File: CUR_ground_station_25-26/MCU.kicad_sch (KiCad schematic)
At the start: 13 parts, among them J4 Conn_01x04_Pin, SW7 PTS815SJM250SMTRLFS, SW8 PTS815SJM250SMTRLFS, U1 ESP32-S3-MINI-1

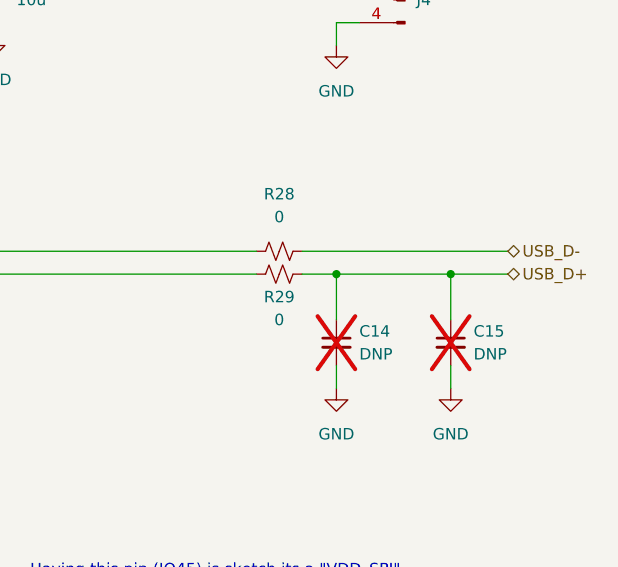
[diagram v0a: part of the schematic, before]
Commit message: Fix USB capacitors
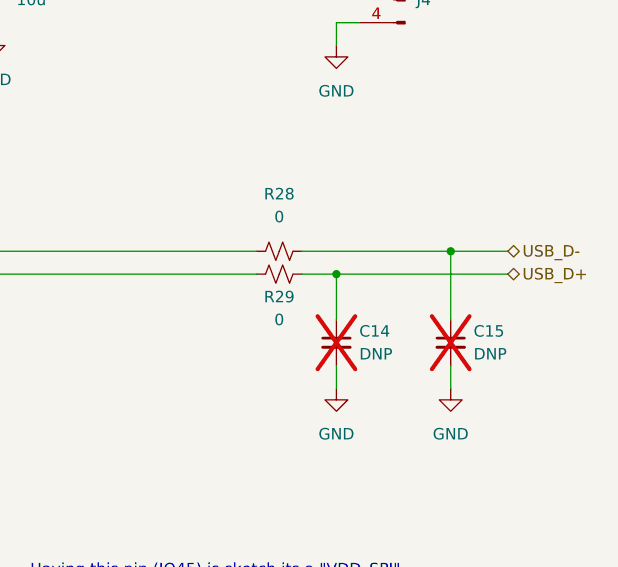
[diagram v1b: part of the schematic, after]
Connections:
- net USB_D+: no longer C15.1
- net USB_D-: now also C15.1
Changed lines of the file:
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@@
+	)
+	(junction
+		(at 234.95 86.36)
+		(diameter 0)
+		(color 0 0 0 0)
 	)
 	(junction
@@
 	)
 	(junction
-		(at 234.95 88.9)
-		(diameter 0)
-		(color 0 0 0 0)
-	)
-	(junction
 		(at 222.25 88.9)
 		(diameter 0)
@@
 	(wire
 		(pts
+			(xy 234.95 86.36) (xy 241.3 86.36)
+		)
+		(stroke
+			(width 0)
+			(type default)
+		)
+	)
+	(wire
+		(pts
 			(xy 130.81 96.52) (xy 137.16 96.52)
 		)
@@
 	(wire
 		(pts
-			(xy 222.25 88.9) (xy 234.95 88.9)
-		)
-		(stroke
-			(width 0)
-			(type default)
-		)
-	)
-	(wire
-		(pts
-			(xy 234.95 88.9) (xy 241.3 88.9)
+			(xy 222.25 88.9) (xy 241.3 88.9)
 		)
 		(stroke
@@
 	(wire
 		(pts
-			(xy 234.95 93.98) (xy 234.95 88.9)
-		)
-		(stroke
-			(width 0)
-			(type default)
-		)
-	)
-	(wire
-		(pts
 			(xy 167.64 104.14) (xy 172.72 104.14)
 		)
@@
 	(wire
 		(pts
+			(xy 234.95 86.36) (xy 234.95 93.98)
+		)
+		(stroke
+			(width 0)
+			(type default)
+		)
+	)
+	(wire
+		(pts
 			(xy 127 78.74) (xy 137.16 78.74)
 		)
@@
 	(wire
 		(pts
-			(xy 218.44 86.36) (xy 241.3 86.36)
-		)
-		(stroke
+			(xy 218.44 86.36) (xy 234.95 86.36)
+		)
+		(stroke

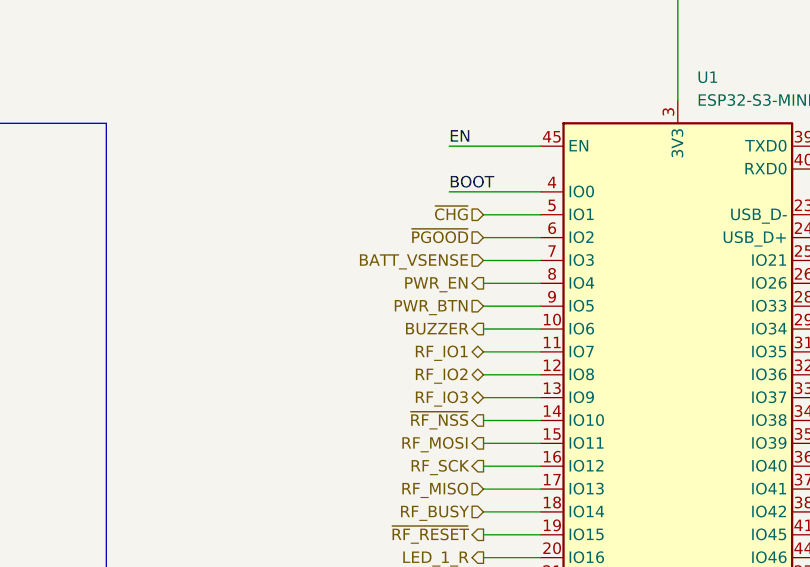
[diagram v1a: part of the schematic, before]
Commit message: switched battery connector, put mounting holes in place
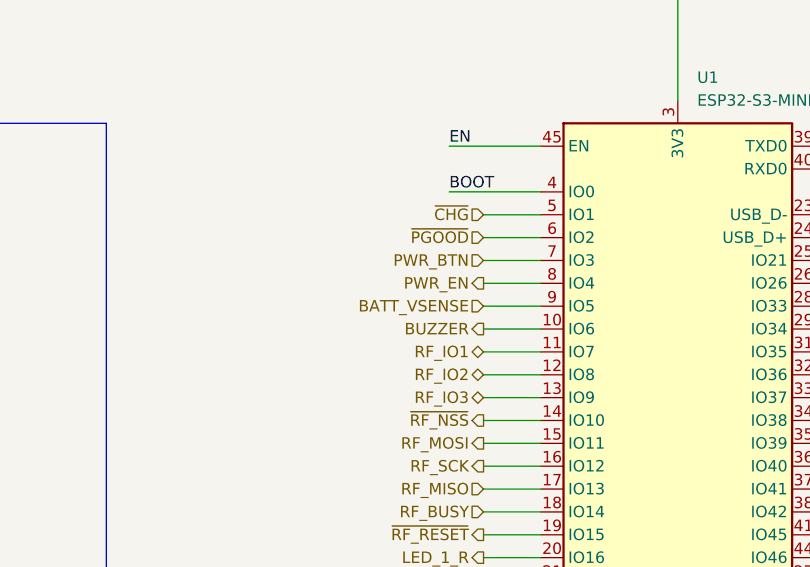
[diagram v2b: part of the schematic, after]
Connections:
- net BATT_VSENSE: now also U1.9 (IO5); no longer U1.7 (IO3)
- net PWR_BTN: now also U1.7 (IO3); no longer U1.9 (IO5)
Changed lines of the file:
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@@
 		)
 	)
-	(hierarchical_label "PWR_BTN"
+	(hierarchical_label "LED_1_B"
+		(shape output)
+		(at 130.81 129.54 180)
+		(effects
+			(font
+				(size 1.27 1.27)
+			)
+			(justify right)
+		)
+	)
+	(hierarchical_label "DISP_~{RES}"
+		(shape output)
+		(at 172.72 116.84 0)
+		(effects
+			(font
+				(size 1.27 1.27)
+			)
+			(justify left)
+		)
+	)
+	(hierarchical_label "DISP_SCL"
+		(shape output)
+		(at 172.72 109.22 0)
+		(effects
+			(font
+				(size 1.27 1.27)
+			)
+			(justify left)
+		)
+	)
+	(hierarchical_label "BTN_3"
+		(shape input)
+		(at 172.72 127 0)
+		(effects
+			(font
+				(size 1.27 1.27)
+			)
+			(justify left)
+		)
+	)
+	(hierarchical_label "RF_MISO"
+		(shape input)
+		(at 130.81 116.84 180)
+		(effects
+			(font
+				(size 1.27 1.27)
+			)
+			(justify right)
+		)
+	)
+	(hierarchical_label "BATT_VSENSE"
 		(shape input)
 		(at 130.81 96.52 180)
-		(effects
-			(font
-				(size 1.27 1.27)
-			)
-			(justify right)
-		)
-	)
-	(hierarchical_label "LED_1_B"
-		(shape output)
-		(at 130.81 129.54 180)
-		(effects
-			(font
-				(size 1.27 1.27)
-			)
-			(justify right)
-		)
-	)
-	(hierarchical_label "DISP_~{RES}"
-		(shape output)
-		(at 172.72 116.84 0)
-		(effects
-			(font
-				(size 1.27 1.27)
-			)
-			(justify left)
-		)
-	)
-	(hierarchical_label "DISP_SCL"
-		(shape output)
-		(at 172.72 109.22 0)
-		(effects
-			(font
-				(size 1.27 1.27)
-			)
-			(justify left)
-		)
-	)
-	(hierarchical_label "BTN_3"
-		(shape input)
-		(at 172.72 127 0)
-		(effects
-			(font
-				(size 1.27 1.27)
-			)
-			(justify left)
-		)
-	)
-	(hierarchical_label "RF_MISO"
-		(shape input)
-		(at 130.81 116.84 180)
 		(effects
 			(font
@@
 		)
 	)
-	(hierarchical_label "BATT_VSENSE"
+	(hierarchical_label "RF_TXEN"
+		(shape input)
+		(at 172.72 93.98 0)
+		(effects
+			(font
+				(size 1.27 1.27)
+			)
+			(justify left)
+		)
+	)
+	(hierarchical_label "DISP_BUSY"
+		(shape input)
+		(at 172.72 114.3 0)
+		(effects
+			(font
+				(size 1.27 1.27)
+			)
+			(justify left)
+		)
+	)
+	(hierarchical_label "LED_2_B"
+		(shape output)
+		(at 172.72 101.6 0)
+		(effects
+			(font
+				(size 1.27 1.27)
+			)
+			(justify left)
+		)
+	)
+	(hierarchical_label "PWR_BTN"
 		(shape input)
 		(at 130.81 91.44 180)
@@
 		)
 	)
-	(hierarchical_label "RF_TXEN"
-		(shape input)
-		(at 172.72 93.98 0)
-		(effects
-			(font
-				(size 1.27 1.27)
-			)
-			(justify left)
-		)
-	)
-	(hierarchical_label "DISP_BUSY"
-		(shape input)
-		(at 172.72 114.3 0)
-		(effects
-			(font
-				(size 1.27 1.27)
-			)
-			(justify left)
-		)
-	)
-	(hierarchical_label "LED_2_B"
-		(shape output)
-		(at 172.72 101.6 0)
-		(effects
-			(font
-				(size 1.27 1.27)
-			)
-			(justify left)
-		)
-	)

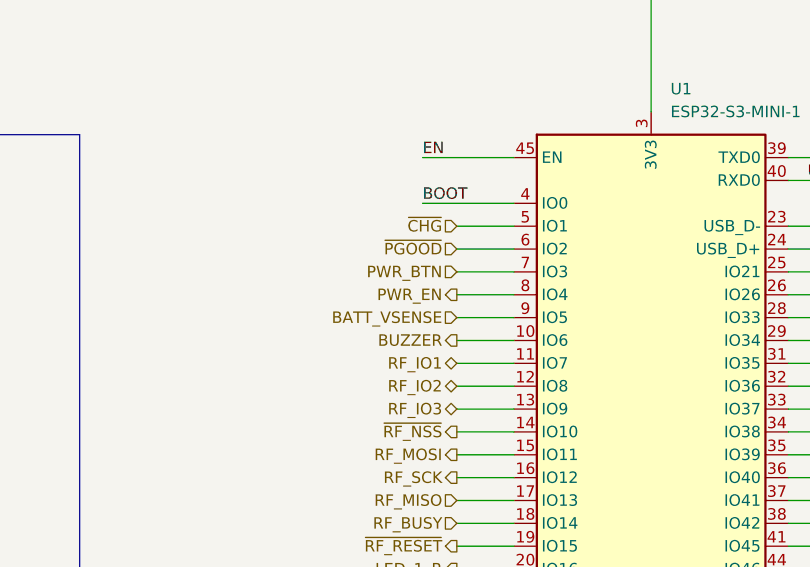
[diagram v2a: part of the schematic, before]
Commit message: routing power section
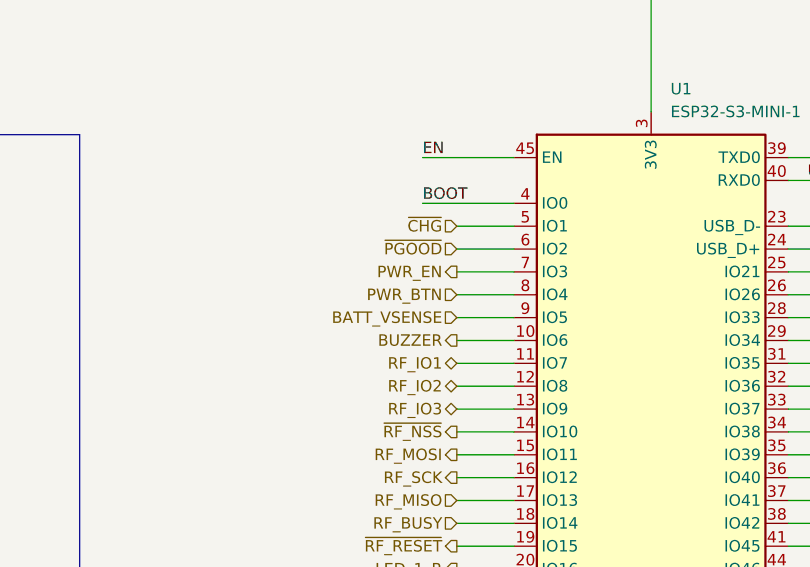
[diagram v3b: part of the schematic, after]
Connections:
- net PWR_BTN: now also U1.8 (IO4); no longer U1.7 (IO3)
- net PWR_EN: now also U1.7 (IO3); no longer U1.8 (IO4)
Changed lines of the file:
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@@
-		)
-	)
-	(hierarchical_label "PWR_BTN"
-		(shape input)
-		(at 130.81 91.44 180)
-		(effects
-			(font
-				(size 1.27 1.27)
-			)
-			(justify right)
 		)
 	)
@@
 		(shape output)
 		(at 130.81 127 180)
+		(effects
+			(font
+				(size 1.27 1.27)
+			)
+			(justify right)
+		)
+	)
+	(hierarchical_label "PWR_BTN"
+		(shape input)
+		(at 130.81 93.98 180)
 		(effects
 			(font
@@
 		)
 	)
-	(hierarchical_label "PWR_EN"
+	(hierarchical_label "BUZZER"
 		(shape output)
-		(at 130.81 93.98 180)
+		(at 130.81 99.06 180)
 		(effects
 			(font
@@
 		)
 	)
-	(hierarchical_label "BUZZER"
+	(hierarchical_label "PWR_EN"
 		(shape output)
-		(at 130.81 99.06 180)
+		(at 130.81 91.44 180)
 		(effects
 			(font

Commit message: signal routing
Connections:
- net BATT_VSENSE: now also U1.8 (IO4); no longer U1.9 (IO5)
- net BUZZER: now also U1.5 (IO1); no longer U1.10 (IO6)
- net DISP_BUSY: now also U1.32 (IO36); no longer U1.36 (IO40)
- net DISP_CS: now also U1.34 (IO38); no longer U1.33 (IO37)
- net DISP_D/~{C}: now also U1.37 (IO41); no longer U1.32 (IO36)
- net DISP_SCL: now also U1.36 (IO40); no longer U1.34 (IO38)
- net DISP_~{RES}: now also U1.33 (IO37); no longer U1.37 (IO41)
- net LED_1_B: now also U1.31 (IO35); no longer U1.22 (IO18)
- net LED_1_G: now also U1.29 (IO34); no longer U1.21 (IO17)
- net LED_1_R: now also U1.28 (IO33); no longer U1.20 (IO16)
- net LED_2_B: now also U1.20 (IO16); no longer U1.31 (IO35)
- net LED_2_G: now also U1.21 (IO17); no longer U1.29 (IO34)
- net LED_2_R: now also U1.22 (IO18); no longer U1.28 (IO33)
- net PWR_BTN: now also U1.10 (IO6); no longer U1.8 (IO4)
- net PWR_EN: now also U1.9 (IO5); no longer U1.7 (IO3)
- net RF_IO1: now also U1.13 (IO9); no longer U1.11 (IO7)
- net RF_IO3: now also U1.11 (IO7); no longer U1.13 (IO9)
- net ~{CHG}: now also U1.6 (IO2); no longer U1.5 (IO1)
- net ~{PGOOD}: now also U1.7 (IO3); no longer U1.6 (IO2)

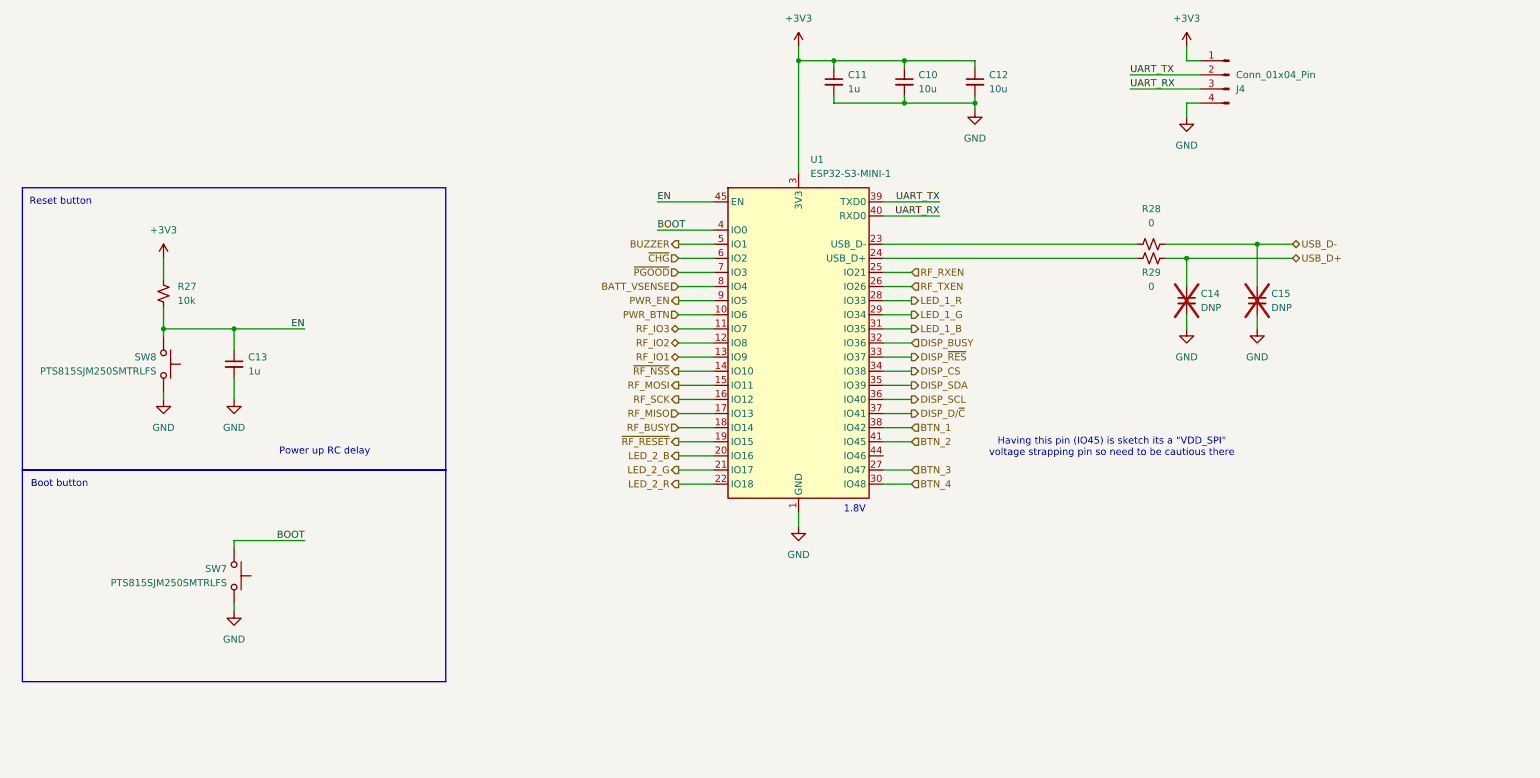
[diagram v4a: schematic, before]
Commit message: Find MPNs again
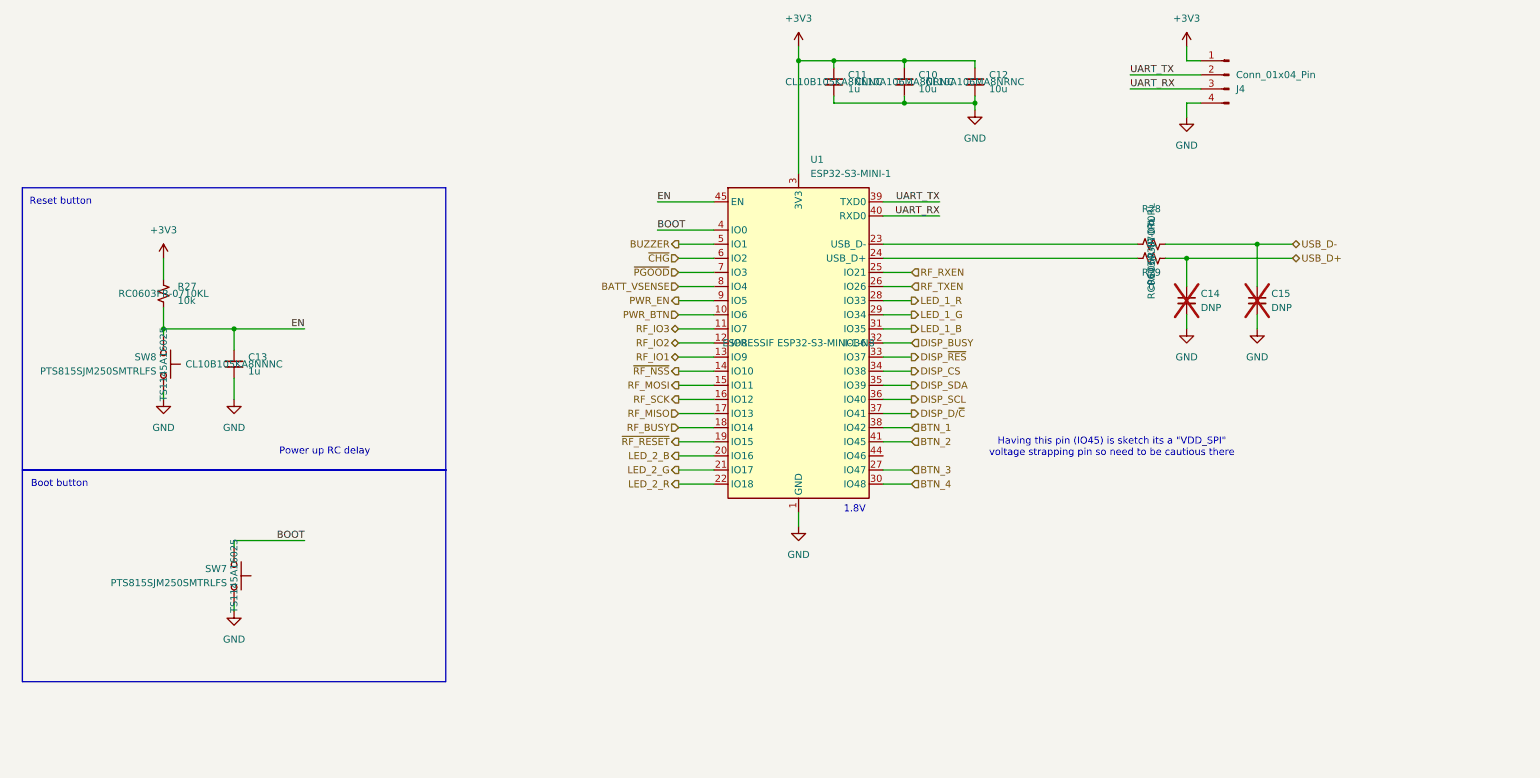
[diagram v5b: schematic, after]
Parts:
- C10, C12: MPN (none) -> CL10A106MA8NRNC
- C11, C13: MPN (none) -> CL10B105KA8NNNC
- J4: now left out of the parts list
- R27: MPN (none) -> RC0603FR-0710KL
- R28, R29: MPN (none) -> RC0603JR-070RL
- SW7, SW8: MPN (none) -> TS1145A16025
- U1: MPN (none) -> ESPRESSIF ESP32-S3-MINI-1-N8
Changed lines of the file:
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@@
+			)
+		)
+		(property "MPN" "CL10A106MA8NRNC"
+			(at 184.15 57.15 0)
+			(effects
+				(font
+					(size 1.27 1.27)
+				)
 			)
 		)
@@
 		(unit 1)
 		(exclude_from_sim no)
-		(in_bom yes)
+		(in_bom no)
 		(on_board yes)
 		(dnp no)
@@
 			)
 		)
+		(property "MPN" " RC0603JR-070RL"
+			(at 215.9 88.9 0)
+			(effects
+				(font
+					(size 1.27 1.27)
+				)
+			)
+		)
 		(pin "1"
 		)
@@
 			)
 		)
+		(property "MPN" " RC0603JR-070RL"
+			(at 215.9 86.36 0)
+			(effects
+				(font
+					(size 1.27 1.27)
+				)
+			)
+		)
 		(pin "1"
 		)
@@
 			)
 		)
+		(property "MPN" "CL10B105KA8NNNC"
+			(at 50.8 107.95 0)
+			(effects
+				(font
+					(size 1.27 1.27)
+				)
+			)
+		)
 		(pin "1"
 		)
@@
 			)
 		)
+		(property "MPN" "CL10A106MA8NRNC"
+			(at 171.45 57.15 0)
+			(effects
+				(font
+					(size 1.27 1.27)
+				)
+			)
+		)
 		(pin "2"
 		)
@@
 				)
 				(hide yes)
+			)
+		)
+		(property "MPN" "CL10B105KA8NNNC"
+			(at 158.75 57.15 0)
+			(effects
+				(font
+					(size 1.27 1.27)
+				)
 			)
 		)
@@
 			)
 		)
+		(property "MPN" "TS1145A16025"
+			(at 50.8 146.05 0)
+			(effects
+				(font
+					(size 1.27 1.27)
+				)
+			)
+		)
 		(pin "1"
 		)
@@
 			)
 		)
+		(property "MPN" "TS1145A16025"
+			(at 38.1 107.95 0)
+			(effects
+				(font
+					(size 1.27 1.27)
+				)
+			)
+		)
 		(pin "1"
 		)
@@
 			)
 		)
+		(property "MPN" "ESPRESSIF ESP32-S3-MINI-1-N8"
+			(at 152.4 104.14 0)
+			(effects
+				(font
+					(size 1.27 1.27)
+				)
+			)
+		)
 		(pin "14"
 		)
@@
 			)
 		)
+		(property "MPN" "RC0603FR-0710KL"
+			(at 38.1 95.25 0)
+			(effects
+				(font
+					(size 1.27 1.27)
+				)
+			)
+		)

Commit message: changes
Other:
- note removed: "Having this pin (IO45) is sketch its a "VDD_SPI" voltage strapping pin so need to be cautious there"
- company: (none) -> Clarkson University Rocketry
- title: (none) -> Ground Station
- moved on the sheet: C13, R27, SW7, SW8
